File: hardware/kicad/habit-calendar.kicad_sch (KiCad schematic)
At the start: 80 parts, among them J1 Conn_01x01, J10 Conn_01x01, J12 Conn_01x01, J13 Conn_01x01, J15 Conn_01x01, J16 Conn_01x01, J17 Conn_01x01, J18 Conn_01x01, J19 Conn_01x01, J2 Conn_01x01, J20 Conn_01x01, J21 Conn_01x01, J22 Conn_01x01, J23 Conn_01x01, J24 Conn_01x01, J25 Conn_01x01, J3 Conn_01x01, J30 Conn_01x06, J4 Conn_01x06, J6 Conn_01x01, J7 Conn_01x01, J8 Conn_01x01, J9 Conn_01x01, SW1 TS-1187A-B-A-B, SW10 TS-1187A-B-A-B, SW11 TS-1187A-B-A-B, SW12 TS-1187A-B-A-B, SW2 TS-1187A-B-A-B, SW3 TS-1187A-B-A-B, SW4 TS-1187A-B-A-B, SW5 TS-1187A-B-A-B, SW6 TS-1187A-B-A-B, SW7 TS-1187A-B-A-B, SW8 TS-1187A-B-A-B, SW9 TS-1187A-B-A-B, U1 PY32F002AF15P6TU

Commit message: One micor ready. About to double the board.
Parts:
- removed J19, J21, J24, J25: Conn_01x01, Connector_PinHeader_2.54mm:PinHeader_1x01_P2.54mm_Vertical, symbol Connector_Generic:Conn_01x01
- removed J30, J4: Conn_01x06, Connector_PinHeader_2.54mm:PinHeader_1x06_P2.54mm_Vertical, symbol Connector_Generic:Conn_01x06
- added H1, H2, H3, H4: MountingHole, MountingHole:MountingHole_2.2mm_M2, symbol Mechanical:MountingHole
- added J4, J5: Conn_01x10, Connector_PinHeader_2.54mm:PinHeader_1x10_P2.54mm_Vertical, symbol Connector_Generic:Conn_01x10
- added J? (x12): Conn_01x01, Connector_PinHeader_2.54mm:PinHeader_1x01_P2.54mm_Vertical, symbol Connector_Generic:Conn_01x01
- added R20, R21, R22, R23: 0 ohm, Resistor_SMD:R_0402_1005Metric, symbol Device:R_Small
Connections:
- net +5V: now also J4.10 (Pin_10), J4.8 (Pin_8), J4.9 (Pin_9), J5.10 (Pin_10), J5.8 (Pin_8), J5.9 (Pin_9)
- net GND: now also J4.5 (Pin_5), J4.6 (Pin_6), J4.7 (Pin_7), J5.5 (Pin_5), J5.6 (Pin_6), J5.7 (Pin_7)
- net PA13: now also J4.4 (Pin_4), R20.2
- net PA14: now also J4.3 (Pin_3), R21.2
- net PF0: now also J4.2 (Pin_2), R22.2
- net PF1: now also J4.1 (Pin_1), R23.2
- net at LED1.2 (DOU): now also LED2.4 (DIN), J?.1 (Pin_1); no longer J22.1 (Pin_1)
- net at LED2.2 (DOU): now also LED3.4 (DIN), J?.1 (Pin_1); no longer LED1.4 (DIN)
- net at LED5.4 (DIN), LED6.2 (DOU): now also J?.1 (Pin_1)
- net at LED6.4 (DIN), LED7.2 (DOU): now also J?.1 (Pin_1)
- net SW8: now reaches J12.1 (Pin_1), R13.1, SW8.1 (A), SW8.2 (B)
- net SW8: now also U1.11 (PA0); no longer U1.14 (PA3)
- net at LED7.4 (DIN), LED8.2 (DOU): now also J?.1 (Pin_1)
- net at LED9.2 (DOU): now also LED10.4 (DIN), J?.1 (Pin_1); no longer LED8.4 (DIN)
- net SW6: now reaches J9.1 (Pin_1), R10.1, SW6.1 (A), SW6.2 (B)
- net SW6: now also U1.7 (PA5); no longer U1.15 (PA4)
- net at R14.1: now also J5.1 (Pin_1)
- net SW12: now reaches J20.1 (Pin_1), R19.1, SW12.1 (A), SW12.2 (B)
- net SW12: now also U1.15 (PA4); no longer U1.11 (PA0)
- net at R5.1: now also J5.3 (Pin_3)
- net SW9: now reaches J16.1 (Pin_1), R15.1, SW9.1 (A), SW9.2 (B)
- net SW9: now also U1.14 (PA3); no longer U1.7 (PA5)
- net at LED3.2 (DOU): now also LED4.4 (DIN), J?.1 (Pin_1); no longer LED2.4 (DIN)
- net at LED4.2 (DOU): now also LED8.4 (DIN), J?.1 (Pin_1); no longer LED3.4 (DIN)
- net at R12.1: now also J5.2 (Pin_2)
- net at R4.1: now also J5.4 (Pin_4)
- net at LED11.2 (DOU): now also LED12.4 (DIN), J?.1 (Pin_1); no longer LED10.4 (DIN)
- net at LED11.4 (DIN): now also LED10.2 (DOU), J?.1 (Pin_1); no longer LED12.2 (DOU)
- net at J23.1 (Pin_1): now also LED12.2 (DOU); no longer LED12.4 (DIN)
- net at LED9.4 (DIN): now also LED5.2 (DOU), J?.1 (Pin_1); no longer LED10.2 (DOU)
- new net WS2812b - Din: J22.1 (Pin_1), J?.1 (Pin_1), LED1.4 (DIN), R20.1, R21.1, R22.1, R23.1
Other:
- note added: "Entering connecter. Extra pwr and gnd to get the power across with room to spare. Internet says 3A ish per pin."
- note added: "Leaving connector. Zero ohm resistors in case disconnection was desirable for whatever reason"
- note added: "Separate LEDs controlled by the master device. Optionally controlled by MCU via zero ohm resistors below. Adds through holes to each Din to have alternative access."
- note added: "Swap switch 8 and 9 to make routing easier. Swap switch 6 and 12 to make routing easier. Should have been more diligint earlier."
- note removed: "Entering connecter"
- note removed: "LEaving connector. Zero ohm resistors in case disconnection was desirable for whatever reason"
- note removed: "Separate LEDs controlled by the master device. Isolated from MCU."
- moved on the sheet: J22, J23, R12, R14, R4, R5

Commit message: Got it. Just needs a logo.
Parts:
- gave numbers to parts that had none: 12
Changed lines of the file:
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@@
   (symbol (lib_id "Connector_Generic:Conn_01x01") (at 127 53.975 0) (unit 1)
     (in_bom yes) (on_board yes)
-    (property "Reference" "J?" (id 0) (at 126.365 58.42 0)
+    (property "Reference" "J29" (id 0) (at 126.365 58.42 0)
       (effects (font (size 1.27 1.27)) (justify left))
     )
@@
   (symbol (lib_id "Connector_Generic:Conn_01x01") (at 202.565 53.975 0) (unit 1)
     (in_bom yes) (on_board yes)
-    (property "Reference" "J?" (id 0) (at 201.93 58.42 0)
+    (property "Reference" "J31" (id 0) (at 201.93 58.42 0)
       (effects (font (size 1.27 1.27)) (justify left))
     )
@@
   (symbol (lib_id "Connector_Generic:Conn_01x01") (at 88.9 29.21 0) (unit 1)
     (in_bom yes) (on_board yes)
-    (property "Reference" "J?" (id 0) (at 88.265 33.655 0)
+    (property "Reference" "J14" (id 0) (at 88.265 33.655 0)
       (effects (font (size 1.27 1.27)) (justify left))
     )
@@
   (symbol (lib_id "Connector_Generic:Conn_01x01") (at 51.435 29.21 0) (unit 1)
     (in_bom yes) (on_board yes)
-    (property "Reference" "J?" (id 0) (at 50.8 33.655 0)
+    (property "Reference" "J11" (id 0) (at 50.8 33.655 0)
       (effects (font (size 1.27 1.27)) (justify left))
     )
@@
   (symbol (lib_id "Connector_Generic:Conn_01x01") (at 126.365 29.21 0) (unit 1)
     (in_bom yes) (on_board yes)
-    (property "Reference" "J?" (id 0) (at 125.73 33.655 0)
+    (property "Reference" "J19" (id 0) (at 125.73 33.655 0)
       (effects (font (size 1.27 1.27)) (justify left))
     )
@@
   (symbol (lib_id "Connector_Generic:Conn_01x01") (at 163.195 53.975 0) (unit 1)
     (in_bom yes) (on_board yes)
-    (property "Reference" "J?" (id 0) (at 162.56 58.42 0)
+    (property "Reference" "J30" (id 0) (at 162.56 58.42 0)
       (effects (font (size 1.27 1.27)) (justify left))
     )
@@
   (symbol (lib_id "Connector_Generic:Conn_01x01") (at 281.305 29.21 0) (unit 1)
     (in_bom yes) (on_board yes)
-    (property "Reference" "J?" (id 0) (at 280.67 33.655 0)
+    (property "Reference" "J26" (id 0) (at 280.67 33.655 0)
       (effects (font (size 1.27 1.27)) (justify left))
     )
@@
   (symbol (lib_id "Connector_Generic:Conn_01x01") (at 205.74 29.21 0) (unit 1)
     (in_bom yes) (on_board yes)
-    (property "Reference" "J?" (id 0) (at 205.105 33.655 0)
+    (property "Reference" "J24" (id 0) (at 205.105 33.655 0)
       (effects (font (size 1.27 1.27)) (justify left))
     )
@@
   (symbol (lib_id "Connector_Generic:Conn_01x01") (at 50.8 53.975 0) (unit 1)
     (in_bom yes) (on_board yes)
-    (property "Reference" "J?" (id 0) (at 50.165 58.42 0)
+    (property "Reference" "J27" (id 0) (at 50.165 58.42 0)
       (effects (font (size 1.27 1.27)) (justify left))
     )
@@
   (symbol (lib_id "Connector_Generic:Conn_01x01") (at 243.205 29.21 0) (unit 1)
     (in_bom yes) (on_board yes)
-    (property "Reference" "J?" (id 0) (at 242.57 33.655 0)
+    (property "Reference" "J25" (id 0) (at 242.57 33.655 0)
       (effects (font (size 1.27 1.27)) (justify left))
     )
@@
   (symbol (lib_id "Connector_Generic:Conn_01x01") (at 163.195 29.21 0) (unit 1)
     (in_bom yes) (on_board yes)
-    (property "Reference" "J?" (id 0) (at 162.56 33.655 0)
+    (property "Reference" "J21" (id 0) (at 162.56 33.655 0)
       (effects (font (size 1.27 1.27)) (justify left))
     )
@@
   (symbol (lib_id "Connector_Generic:Conn_01x01") (at 90.17 53.975 0) (unit 1)
     (in_bom yes) (on_board yes)
-    (property "Reference" "J?" (id 0) (at 89.535 58.42 0)
+    (property "Reference" "J28" (id 0) (at 89.535 58.42 0)
       (effects (font (size 1.27 1.27)) (justify left))
     )
@@
       (reference "J10") (unit 1) (value "Conn_01x01") (footprint "Connector_PinHeader_2.54mm:PinHeader_1x01_P2.54mm_Vertical")
     )
+    (path "/5e468278-a671-45a3-ae57-3a3915003827"
+      (reference "J11") (unit 1) (value "Conn_01x01") (footprint "Connector_PinHeader_2.54mm:PinHeader_1x01_P2.54mm_Vertical")
+    )
     (path "/1858fa0a-9390-496d-8452-84b68cb91c34"
       (reference "J12") (unit 1) (value "Conn_01x01") (footprint "Connector_PinHeader_2.54mm:PinHeader_1x01_P2.54mm_Vertical")
@@
       (reference "J13") (unit 1) (value "Conn_01x01") (footprint "Connector_PinHeader_2.54mm:PinHeader_1x01_P2.54mm_Vertical")
     )
+    (path "/5313c111-d641-4208-af55-83a1109a311e"
+      (reference "J14") (unit 1) (value "Conn_01x01") (footprint "Connector_PinHeader_2.54mm:PinHeader_1x01_P2.54mm_Vertical")
+    )
     (path "/a8ac1b49-1103-4ba8-a65c-9dd2de02b674"
       (reference "J15") (unit 1) (value "Conn_01x01") (footprint "Connector_PinHeader_2.54mm:PinHeader_1x01_P2.54mm_Vertical")
@@
       (reference "J18") (unit 1) (value "Conn_01x01") (footprint "Connector_PinHeader_2.54mm:PinHeader_1x01_P2.54mm_Vertical")
     )
+    (path "/5f56cda0-698c-44fd-b25e-d04a6d64afdd"
+      (reference "J19") (unit 1) (value "Conn_01x01") (footprint "Connector_PinHeader_2.54mm:PinHeader_1x01_P2.54mm_Vertical")
+    )
     (path "/2d898d12-b4a9-40f4-879b-302363faa6e4"
       (reference "J20") (unit 1) (value "Conn_01x01") (footprint "Connector_PinHeader_2.54mm:PinHeader_1x01_P2.54mm_Vertical")
     )
+    (path "/dc23beb0-97b6-4631-8167-aaa24488ad71"
+      (reference "J21") (unit 1) (value "Conn_01x01") (footprint "Connector_PinHeader_2.54mm:PinHeader_1x01_P2.54mm_Vertical")
+    )
     (path "/6d11ab06-0557-4192-8da1-6c6e07f93ed1"
       (reference "J22") (unit 1) (value "Conn_01x01") (footprint "Connector_PinHeader_2.54mm:PinHeader_1x01_P2.54mm_Vertical")
@@
       (reference "J23") (unit 1) (value "Conn_01x01") (footprint "Connector_PinHeader_2.54mm:PinHeader_1x01_P2.54mm_Vertical")
     )
-    (path "/07d9f221-64df-4dd6-8af0-788d7348aac6"
-      (reference "J?") (unit 1) (value "Conn_01x01") (footprint "Connector_PinHeader_2.54mm:PinHeader_1x01_P2.54mm_Vertical")
-    )
-    (path "/192b1a81-6d59-40f1-b49a-68ae4def9683"
-      (reference "J?") (unit 1) (value "Conn_01x01") (footprint "Connector_PinHeader_2.54mm:PinHeader_1x01_P2.54mm_Vertical")
-    )
-    (path "/5313c111-d641-4208-af55-83a1109a311e"
-      (reference "J?") (unit 1) (value "Conn_01x01") (footprint "Connector_PinHeader_2.54mm:PinHeader_1x01_P2.54mm_Vertical")
-    )
-    (path "/5e468278-a671-45a3-ae57-3a3915003827"
-      (reference "J?") (unit 1) (value "Conn_01x01") (footprint "Connector_PinHeader_2.54mm:PinHeader_1x01_P2.54mm_Vertical")
-    )
-    (path "/5f56cda0-698c-44fd-b25e-d04a6d64afdd"
-      (reference "J?") (unit 1) (value "Conn_01x01") (footprint "Connector_PinHeader_2.54mm:PinHeader_1x01_P2.54mm_Vertical")
+    (path "/8a2107d0-78a5-46f5-a5a8-9ae8b28ce00a"
+      (reference "J24") (unit 1) (value "Conn_01x01") (footprint "Connector_PinHeader_2.54mm:PinHeader_1x01_P2.54mm_Vertical")
     )
-    (path "/62019e93-39b4-4364-ac35-88557f8fe3c6"
-      (reference "J?") (unit 1) (value "Conn_01x01") (footprint "Connector_PinHeader_2.54mm:PinHeader_1x01_P2.54mm_Vertical")
+    (path "/bd978cb0-ea97-4418-8066-299d94ea1edb"
+      (reference "J25") (unit 1) (value "Conn_01x01") (footprint "Connector_PinHeader_2.54mm:PinHeader_1x01_P2.54mm_Vertical")
     )
     (path "/728da411-35d3-4354-8a9c-634cca3c2a7c"
-      (reference "J?") (unit 1) (value "Conn_01x01") (footprint "Connector_PinHeader_2.54mm:PinHeader_1x01_P2.54mm_Vertical")
-    )
-    (path "/8a2107d0-78a5-46f5-a5a8-9ae8b28ce00a"
-      (reference "J?") (unit 1) (value "Conn_01x01") (footprint "Connector_PinHeader_2.54mm:PinHeader_1x01_P2.54mm_Vertical")
+      (reference "J26") (unit 1) (value "Conn_01x01") (footprint "Connector_PinHeader_2.54mm:PinHeader_1x01_P2.54mm_Vertical")
     )
     (path "/99b3bc8c-a9b0-48a9-acec-3154331dcbc0"
-      (reference "J?") (unit 1) (value "Conn_01x01") (footprint "Connector_PinHeader_2.54mm:PinHeader_1x01_P2.54mm_Vertical")
+      (reference "J27") (unit 1) (value "Conn_01x01") (footprint "Connector_PinHeader_2.54mm:PinHeader_1x01_P2.54mm_Vertical")
     )
-    (path "/bd978cb0-ea97-4418-8066-299d94ea1edb"
-      (reference "J?") (unit 1) (value "Conn_01x01") (footprint "Connector_PinHeader_2.54mm:PinHeader_1x01_P2.54mm_Vertical")
+    (path "/f772f759-9341-4345-b12d-4d8664940b62"
+      (reference "J28") (unit 1) (value "Conn_01x01") (footprint "Connector_PinHeader_2.54mm:PinHeader_1x01_P2.54mm_Vertical")
     )
-    (path "/dc23beb0-97b6-4631-8167-aaa24488ad71"
-      (reference "J?") (unit 1) (value "Conn_01x01") (footprint "Connector_PinHeader_2.54mm:PinHeader_1x01_P2.54mm_Vertical")
+    (path "/07d9f221-64df-4dd6-8af0-788d7348aac6"
+      (reference "J29") (unit 1) (value "Conn_01x01") (footprint "Connector_PinHeader_2.54mm:PinHeader_1x01_P2.54mm_Vertical")
     )
-    (path "/f772f759-9341-4345-b12d-4d8664940b62"
-      (reference "J?") (unit 1) (value "Conn_01x01") (footprint "Connector_PinHeader_2.54mm:PinHeader_1x01_P2.54mm_Vertical")
+    (path "/62019e93-39b4-4364-ac35-88557f8fe3c6"
+      (reference "J30") (unit 1) (value "Conn_01x01") (footprint "Connector_PinHeader_2.54mm:PinHeader_1x01_P2.54mm_Vertical")
+    )
+    (path "/192b1a81-6d59-40f1-b49a-68ae4def9683"
+      (reference "J31") (unit 1) (value "Conn_01x01") (footprint "Connector_PinHeader_2.54mm:PinHeader_1x01_P2.54mm_Vertical")
     )
     (path "/099697f8-8bb5-4972-84e2-be14e72ae45e"

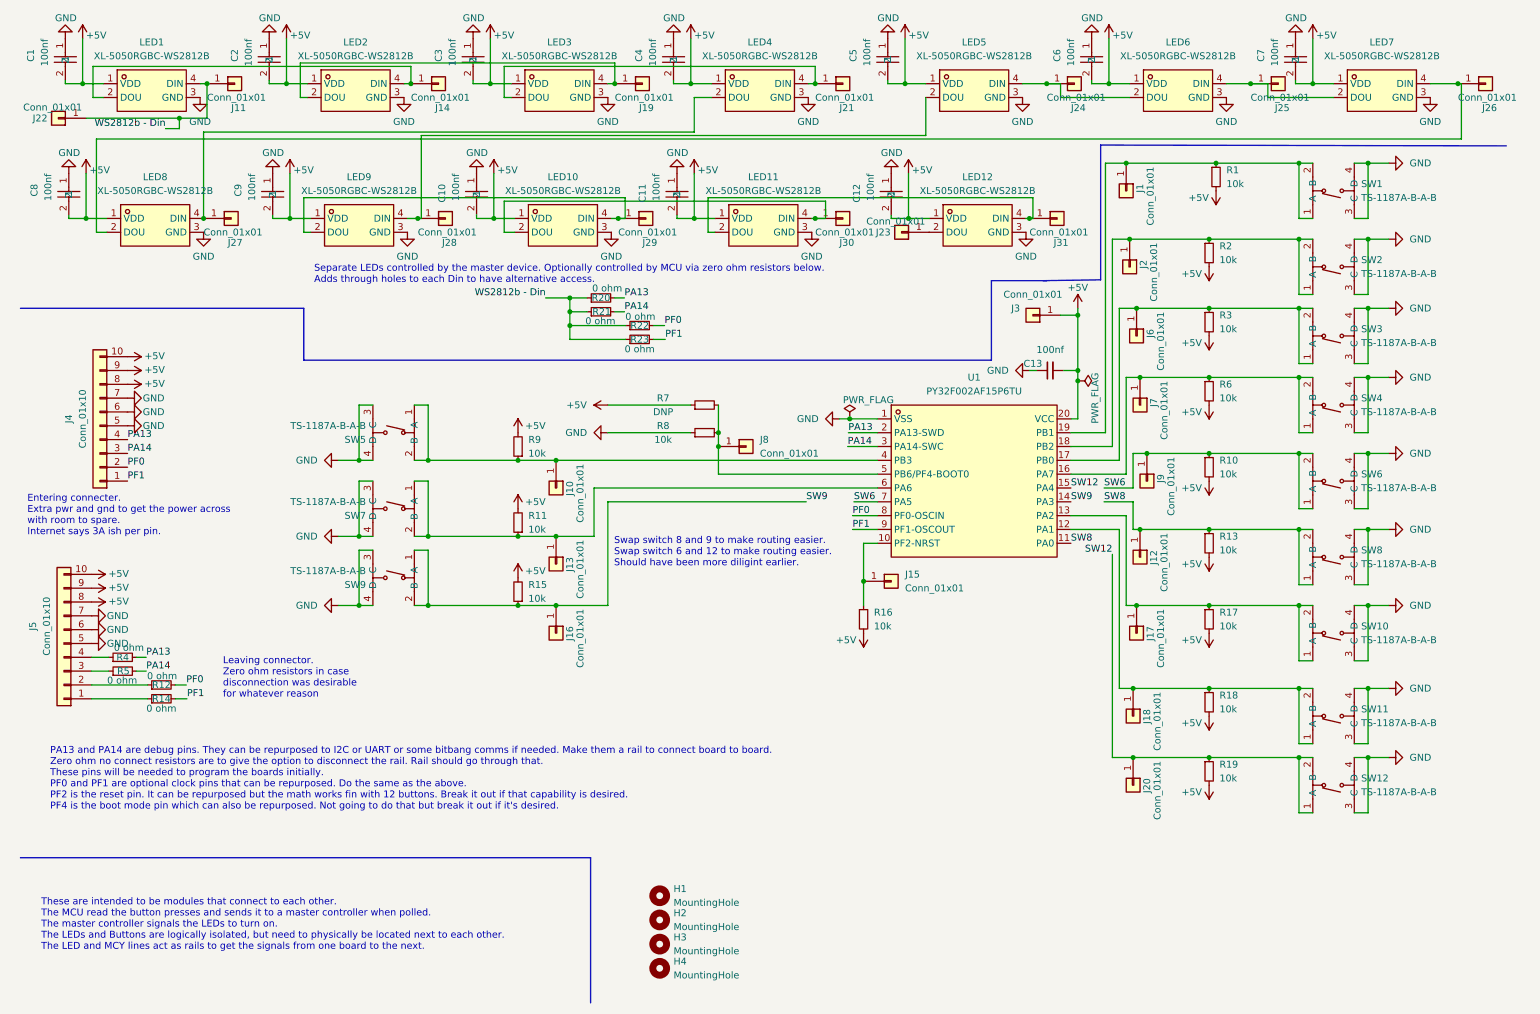
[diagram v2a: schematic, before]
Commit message: Moved to a new heirarchical sheet. Instantiated two. Some PCB tweeks. Added Logo. Now going to use the replicate plugin to make another copy.
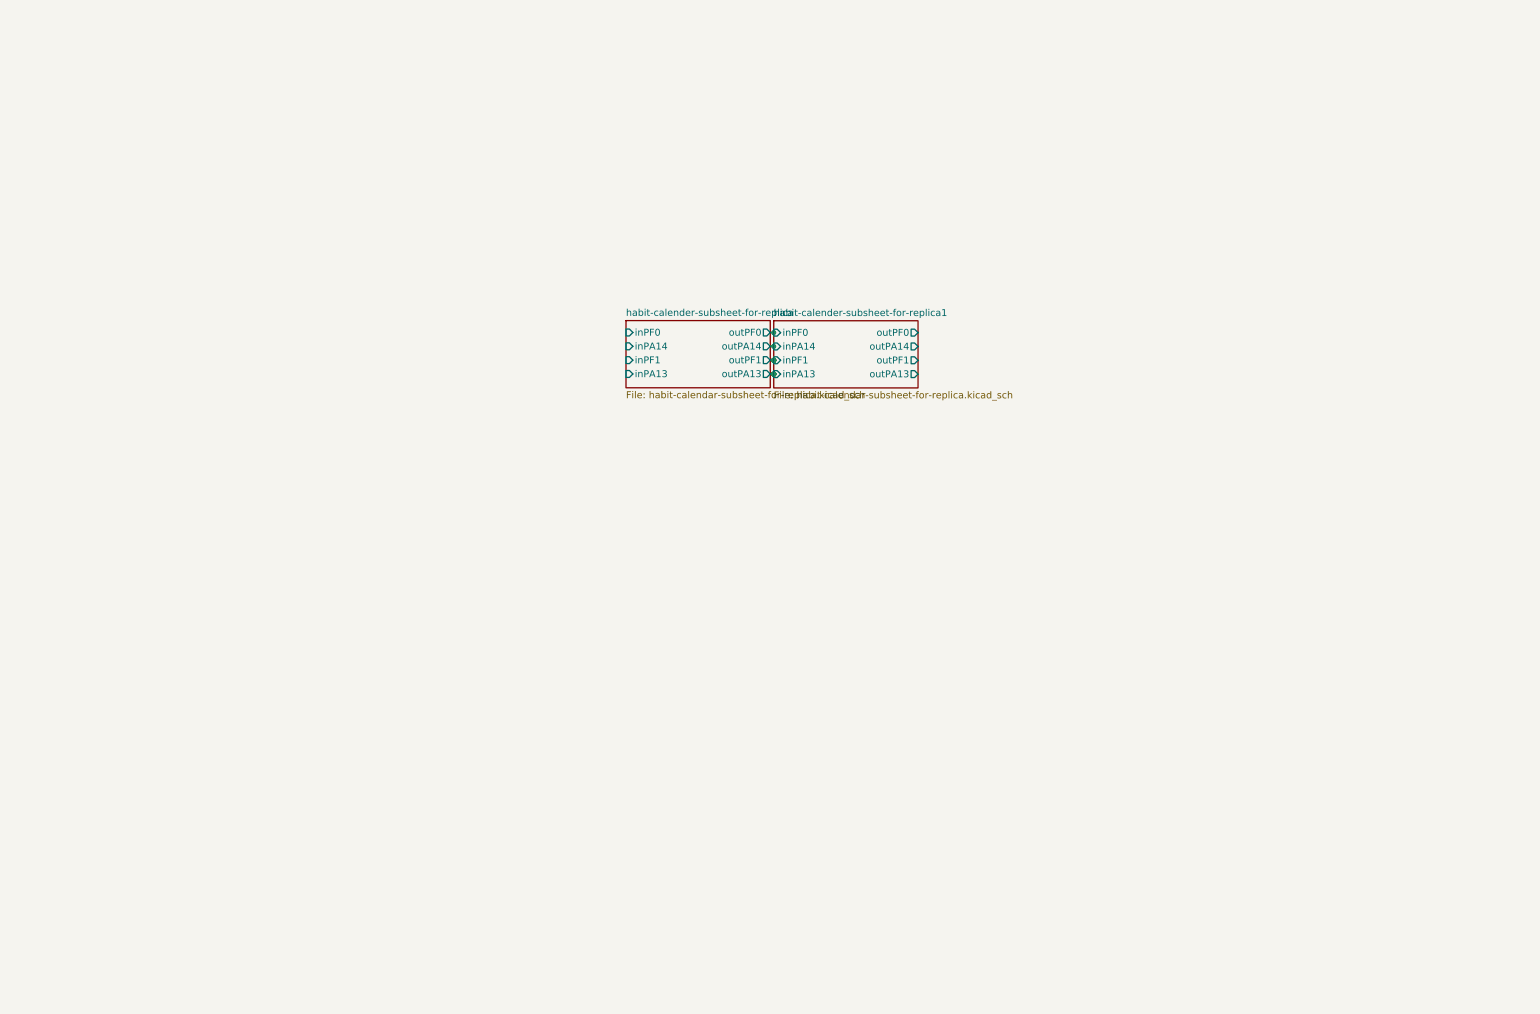
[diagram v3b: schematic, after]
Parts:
- removed C1, C10, C11, C12, C2, C3, C4, C5, C6, C7, C8, C9: 100nf, easyeda2kicadLocal:C0402, symbol easyeda2kicad:CL05B104KO5NNNC
- removed C13: 100nf, easyeda2kicadLocal:C0402, symbol Device:C_Small
- removed H1, H2, H3, H4: MountingHole, MountingHole:MountingHole_2.2mm_M2, symbol Mechanical:MountingHole
- removed J1, J10, J11, J12, J13, J14, J15, J16, J17, J18, J19, J2, J20, J21, J22, J23, J24, J25, J26, J27, J28, J29, J3, J30, J31, J6, J7, J8, J9: Conn_01x01, Connector_PinHeader_2.54mm:PinHeader_1x01_P2.54mm_Vertical, symbol Connector_Generic:Conn_01x01
- removed J4, J5: Conn_01x10, Connector_PinHeader_2.54mm:PinHeader_1x10_P2.54mm_Vertical, symbol Connector_Generic:Conn_01x10
- removed LED1, LED10, LED11, LED12, LED2, LED3, LED4, LED5, LED6, LED7, LED8, LED9: XL-5050RGBC-WS2812B, easyeda2kicadLocal3:LED-SMD_4P-L5.0-W5.0-BL_XL-5050RGBC, symbol easyeda2kicad:XL-5050RGBC-WS2812B
- removed R1, R10, R11, R13, R15, R16, R17, R18, R19, R2, R3, R6, R8, R9: 10k, Resistor_SMD:R_0402_1005Metric, symbol Device:R_Small
- removed R12, R14, R20, R21, R22, R23, R4, R5: 0 ohm, Resistor_SMD:R_0402_1005Metric, symbol Device:R_Small
- removed R7: DNP, Resistor_SMD:R_0402_1005Metric, symbol Device:R_Small
- removed SW1, SW10, SW11, SW12, SW2, SW3, SW4, SW5, SW6, SW7, SW8, SW9: TS-1187A-B-A-B, easyeda2kicad:SW-SMD_4P-L5.1-W5.1-P3.70-LS6.5-TL-2, symbol easyeda2kicad:TS-1187A-B-A-B
- removed U1: PY32F002AF15P6TU, easyeda2kicad:TSSOP-20_L6.5-W4.4-P0.65-LS6.4-BL, symbol easyeda2kicad:PY32F002AF15P6TU
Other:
- added sheet habit-calender-subsheet-for-replica (habit-calendar-subsheet-for-replica.kicad_sch)
- added sheet habit-calender-subsheet-for-replica1 (habit-calendar-subsheet-for-replica.kicad_sch)
- note removed: "Entering connecter. Extra pwr and gnd to get the power across with room to spare. Internet says 3A ish per pin."
- note removed: "Leaving connector. Zero ohm resistors in case disconnection was desirable for whatever reason"
- note removed: "PA13 and PA14 are debug pins. They can be repurposed to I2C or UART or some bitbang comms if needed. Make them a rail to connect board to board. Zero ohm no connect resistors are to give the option to disconnect the rail. Rail should go through that. These pins will be needed to program the boards initially. PF0 and PF1 are optional clock pins that can be repurposed. Do the same as the above. PF2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"
- note removed: "Separate LEDs controlled by the master device. Optionally controlled by MCU via zero ohm resistors below. Adds through holes to each Din to have alternative access."
- note removed: "Swap switch 8 and 9 to make routing easier. Swap switch 6 and 12 to make routing easier. Should have been more diligint earlier."
- note removed: "These are intended to be modules that connect to each other. The MCU read the button presses and sends it to a master controller when polled. The master controller signals the LEDs to turn on. The LEDs and Buttons are logically isolated, but need to physically be located next to each other. The LED and MCY lines act as rails to get the signals from one board to the next."
- title: (none) -> Habit Calendar
